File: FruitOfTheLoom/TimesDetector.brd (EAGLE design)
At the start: 113 x 100 mm, 20 parts, among them K1 RELAY-SPDT-JZC-11F, K2 RELAY-SPDT-JZC-11F

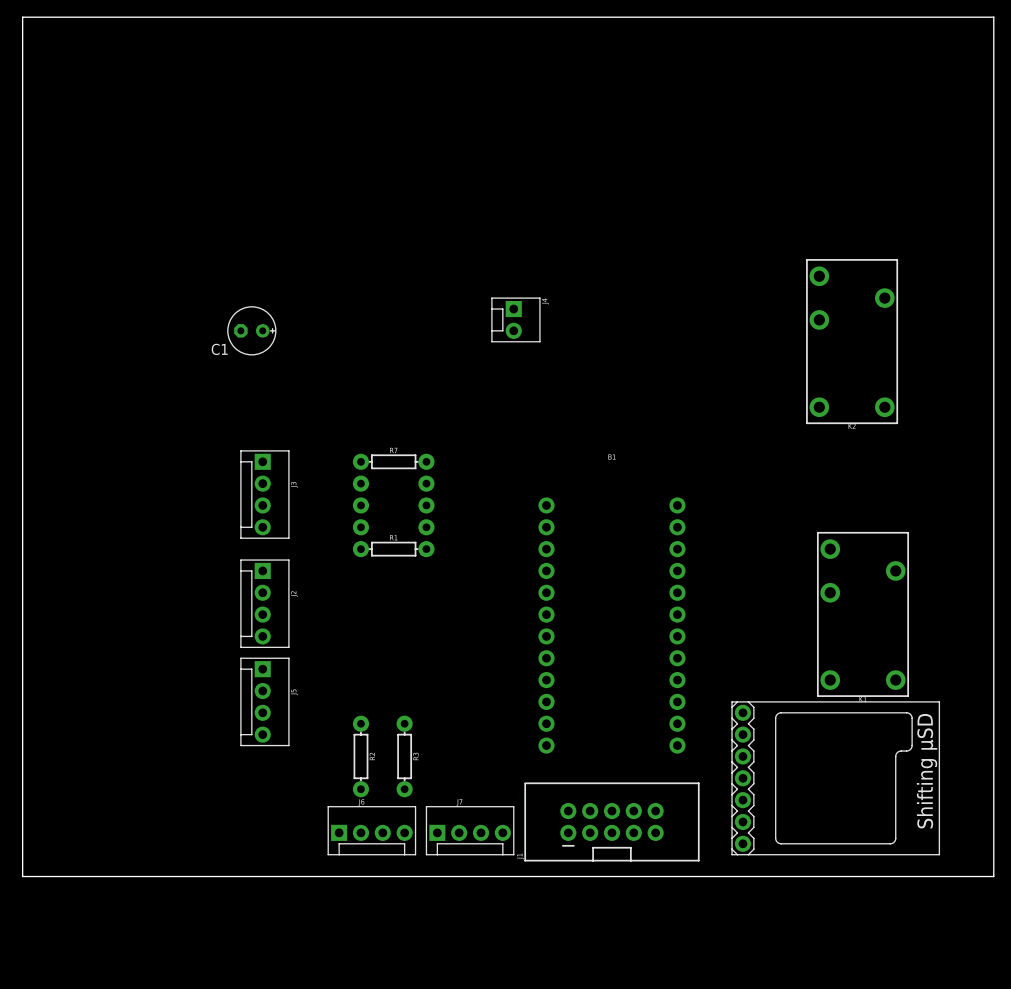
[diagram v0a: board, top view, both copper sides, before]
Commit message: Finalizacion de esquematico, ordenamiento de diseño de placa electronica
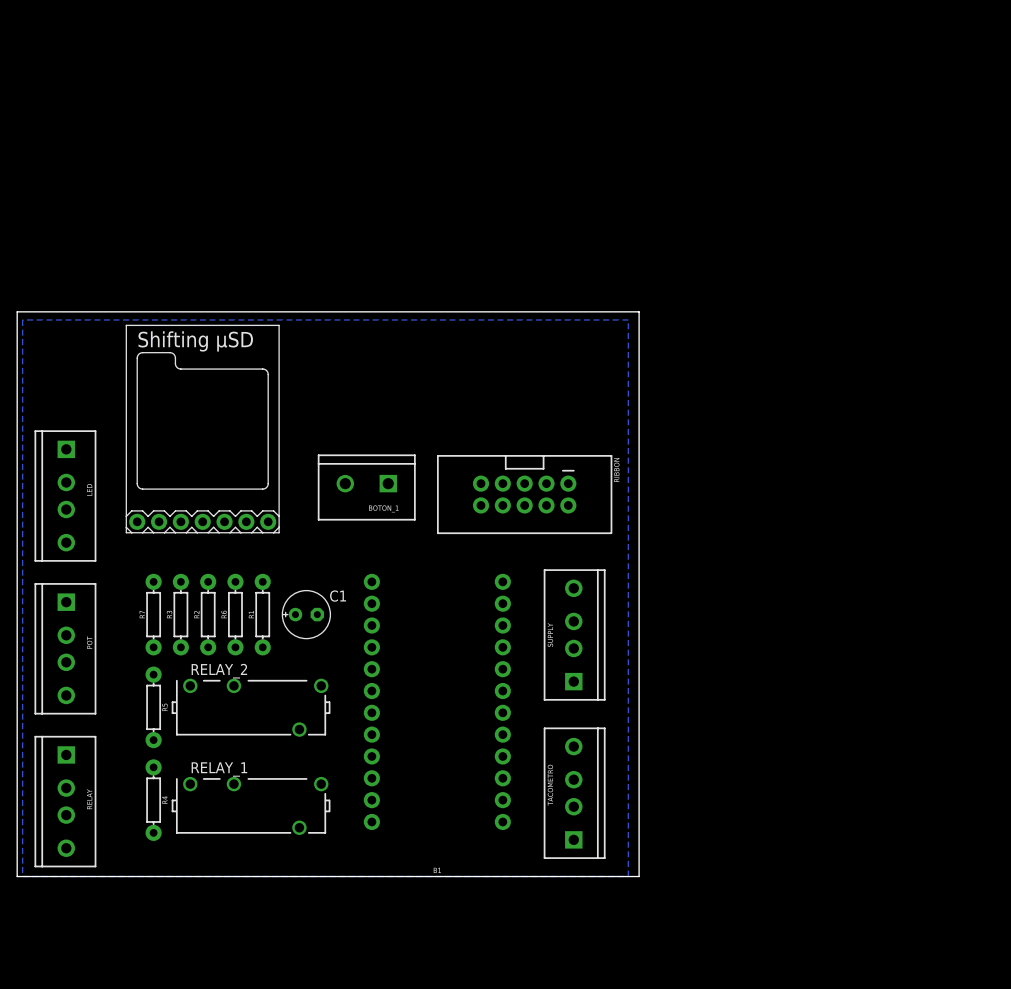
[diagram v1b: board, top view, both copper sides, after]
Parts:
- removed J1: (no value), SparkFun-Connectors:2X5-SHROUDED
- removed J2, J3, J5, J6, J7: (no value), SparkFun-Connectors:MOLEX-1X4
- removed J4: (no value), SparkFun-Connectors:MOLEX-1X2
- removed K1, K2: RELAY-SPDT-JZC-11F, SparkFun-Electromechanical:RELAY-JZC
- added BOTON_1: (no value), SparkFun-Connectors:SCREWTERMINAL-5MM-2
- added LED, POT, RELAY, SUPPLY, TACOMETRO: (no value), SparkFun-Connectors:SCREWTERMINAL-3.5MM-4_LOCK
- added RELAY_1, RELAY_2: G6D-1A-ASI12VDC, relay:G6D
- added RIBBON: (no value), SparkFun-Connectors:2X5-SHROUDED
- C1: value (none) -> 100µ
- moved MODULE1 73.2 mm to (12.1, 40.0), turned to 0 degrees
- moved R4 42.3 mm to (15.2, 8.89), flipped to the top, turned to 270 degrees
- moved R5 36.5 mm to (15.2, 19.7), flipped to the top, turned to 270 degrees
- moved C1 33.6 mm to (33.0, 30.5), turned to 0 degrees
- moved R7 33.1 mm to (15.2, 30.5), turned to 90 degrees
- moved R3 30.8 mm to (18.4, 30.5), turned to 90 degrees
- moved R2 24.3 mm to (21.6, 30.5), turned to 90 degrees
- moved R6 23.9 mm to (24.8, 30.5), flipped to the top, turned to 90 degrees
- moved B1 23.3 mm to (48.3, 19.1), turned to 180 degrees
- moved FRAME1 18.5 mm to (13.3, -8.89)
- moved R1 17.0 mm to (27.9, 30.5), turned to 90 degrees
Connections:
- removed net N$6: MODULE1.P_CD, R6.P$1
- new net N$1: MODULE1.P_CD, R6.P$2
- net A0: now also LED.1; no longer J6.1
- net A1: now also POT.2; no longer J5.2
- net A2: now also RELAY_1.7; no longer K1.4
- net A3: now also R5.P$2, RELAY_2.7; no longer K2.4, R5.P$1
- net D2: now also RIBBON.5; no longer J1.5
- net D3: now also RIBBON.6; no longer J1.6
- net D4: now also RIBBON.7; no longer J1.7
- net D5: now also RIBBON.8; no longer J1.8
- net D6: now also RIBBON.4; no longer J1.4
- net D7: now also RIBBON.3; no longer J1.3
- net D8: now also BOTON_1.2; no longer J4.2
- net D9: now also LED.3; no longer J6.3
- net GND: now also POT.3, R5.P$1, R6.P$1, RELAY.3, RELAY_1.13, RELAY_2.13, RIBBON.9, SUPPLY.2, SUPPLY.4, TACOMETRO.2; no longer J1.9, J2.2, J2.4, J3.2, J5.3, K1.1, K2.1, R5.P$2, R6.P$2
- net IN_SEN_1: now also RELAY.2, RELAY_2.1; no longer J7.2, K1.5
- net IN_SEN_2: now also RELAY.1, RELAY_1.1; no longer J7.1, K2.5
- net N$2: now also LED.4; no longer J6.4
- net N$4: now also LED.2; no longer J6.2
- net N$8: now also R7.P$1, RIBBON.1; no longer J1.1, R7.P$2
- net RX: now also TACOMETRO.3; no longer J3.3
- net TX: now also TACOMETRO.4; no longer J3.4
- net V0: now also POT.4, RIBBON.2; no longer J1.2, J5.4
- net VCC: now also RELAY.4, RELAY_1.5, RELAY_2.5, SUPPLY.1, TACOMETRO.1; no longer J2.1, J3.1, J7.4
- net VCC_O: now also BOTON_1.1, POT.1, R7.P$2, RIBBON.10, SUPPLY.3; no longer J1.10, J2.3, J4.1, J5.1, K1.3, K2.3, R7.P$1
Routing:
- added copper zone on layer 16, net GND
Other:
- board size 113 x 100 mm -> 72.4 x 65.7 mm

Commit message: Orden de los componentes segun el cliente
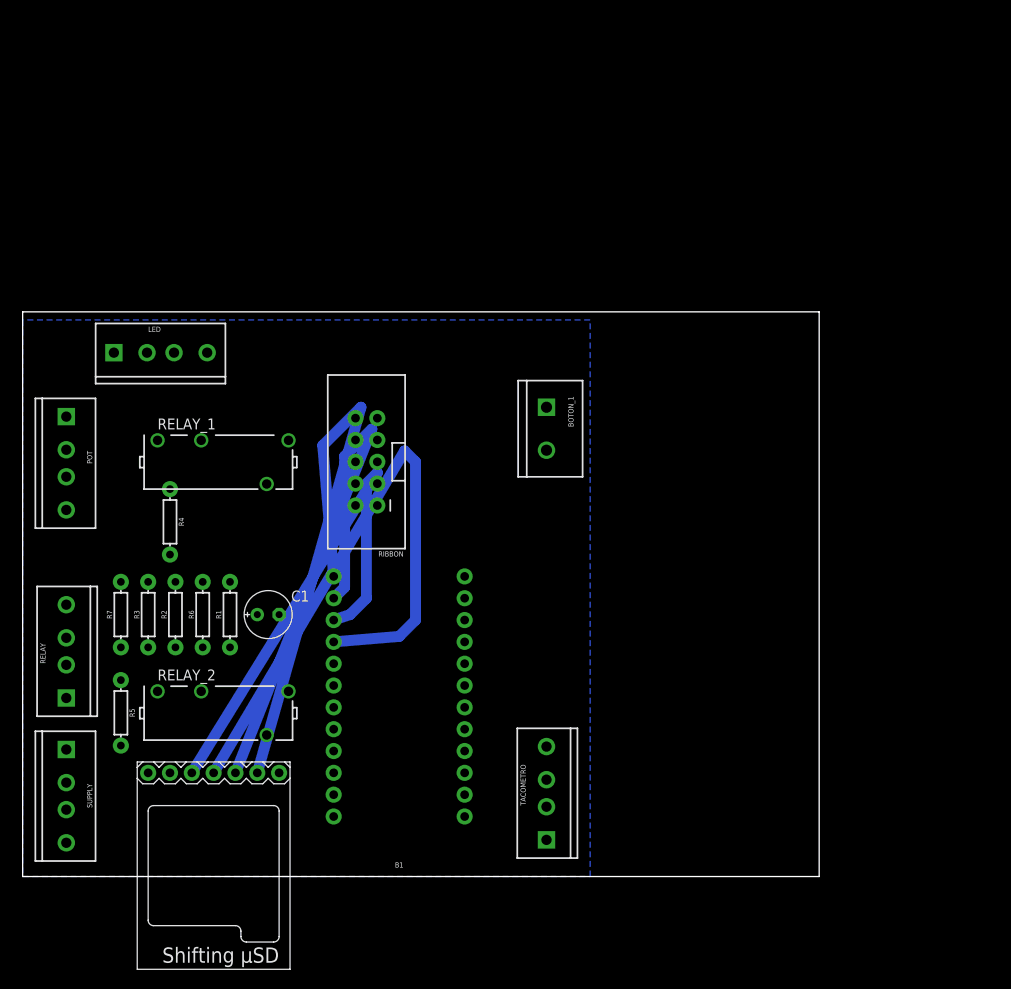
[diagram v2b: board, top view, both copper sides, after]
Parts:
- moved SUPPLY 59.6 mm to (5.08, 14.6), turned to 270 degrees
- moved RELAY_1 40.2 mm to (22.9, 48.3)
- moved MODULE1 32.8 mm to (31.1, 13.3), turned to 180 degrees
- moved R4 32.4 mm to (17.1, 41.3)
- moved POT 21.6 mm to (5.08, 53.3)
- moved BOTON_1 20.4 mm to (61.0, 54.6), turned to 270 degrees
- moved RIBBON 18.8 mm to (40.0, 48.3), turned to 180 degrees
- moved LED 12.8 mm to (10.8, 61.0), turned to 0 degrees
- moved RELAY 6.98 mm to (5.08, 21.0), turned to 90 degrees
- moved B1 4.49 mm to (43.8, 19.7)
- moved C1 4.45 mm to (28.6, 30.5)
- moved RELAY_2 3.86 mm to (22.9, 19.1)
- moved R5 3.86 mm to (11.4, 19.1)
- moved R1 3.81 mm to (24.1, 30.5)
- moved R6 3.81 mm to (21.0, 30.5)
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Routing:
- net D13: track 0.00 -> 74.1 mm
- net D10: track 0.00 -> 65.8 mm
- net D11: track 0.00 -> 64.6 mm
- net D12: track 0.00 -> 60.9 mm
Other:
- board size 72.4 x 65.7 mm -> 92.7 x 65.7 mm

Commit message: Finalizacion de diseño de circuito, fase de revision
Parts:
- added FRAME3: FRAME-LETTERNO_PACKAGE, SparkFun-Aesthetics:DUMMY
- added J2: (no value), SparkFun-Connectors:1X05_LONGPADS
- moved RELAY_2 51.0 mm to (66.7, 45.1), turned to 90 degrees
- moved R5 45.8 mm to (51.4, 41.3)
- moved R1 42.0 mm to (66.0, 33.7), turned to 180 degrees
- moved C1 36.3 mm to (64.8, 27.3), turned to 270 degrees
- moved RELAY_1 35.1 mm to (57.8, 45.1), turned to 90 degrees
- moved R4 29.8 mm to (47.0, 41.3), turned to 90 degrees
- moved R7 29.4 mm to (8.26, 59.7), turned to 180 degrees
- moved R2 27.7 mm to (8.26, 56.5), turned to 0 degrees
- moved R3 23.7 mm to (8.26, 53.3), turned to 0 degrees
- moved POT 15.9 mm to (6.35, 37.5), turned to 90 degrees
- moved MODULE1 13.1 mm to (36.2, 25.4)
- moved TACOMETRO 12.0 mm to (67.3, 14.6), turned to 270 degrees
- moved SUPPLY 10.9 mm to (6.35, 3.81), turned to 90 degrees
- moved BOTON_1 10.2 mm to (66.0, 63.5)
- moved RELAY 10.2 mm to (6.35, 31.1), turned to 270 degrees
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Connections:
- net D2: now also J2.5
- net D3: now also J2.4
- net D5: now also J2.3
- net D6: now also J2.2
- net D9: now also J2.1
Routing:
- net VCC_O: track 0.00 -> 181.3 mm
- net D2: track 0.00 -> 150.1 mm
- net VCC: track 0.00 -> 144.1 mm
- net IN_SEN_1: track 0.00 -> 113.9 mm
- net IN_SEN_2: track 0.00 -> 94.2 mm
- net D4: track 0.00 -> 77.0 mm
- net D9: track 0.00 -> 66.3 mm
- net V0: track 0.00 -> 65.1 mm
- net A0: track 0.00 -> 61.1 mm
- net D13: track 74.1 -> 16.0 mm
- net D3: track 0.00 -> 57.0 mm
- net A1: track 0.00 -> 53.2 mm
- net D10: track 65.8 -> 15.8 mm
- net D7: track 0.00 -> 49.7 mm
- net A3: track 0.00 -> 46.4 mm
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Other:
- board size 92.7 x 65.7 mm -> 73 x 68.9 mm

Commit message: Finalizacion de diseño de circuito, fase de revision
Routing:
- net VCC_O: track 181.3 -> 182.8 mm
- net A0: track 61.1 -> 61.8 mm
- net A1: track 53.2 -> 54.0 mm
- added copper zone on layer 1, net GND
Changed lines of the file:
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@@
 <contactref element="R5" pad="P$1"/>
 <contactref element="RELAY" pad="3"/>
-<polygon width="0.1524" layer="16">
+<polygon width="0.1524" layer="16" isolate="0.6096">
 <vertex x="-0.635" y="68.58"/>
 <vertex x="-0.635" y="0"/>
@@
 <contactref element="R6" pad="P$1"/>
 <contactref element="R4" pad="P$2"/>
+<polygon width="0.0762" layer="1" isolate="0.6096">
+<vertex x="-0.635" y="68.58"/>
+<vertex x="-0.635" y="0"/>
+<vertex x="72.39" y="0"/>
+<vertex x="72.39" y="68.58"/>
+</polygon>
 </signal>
 <signal name="RX">
@@
 <wire x1="9.6572" y1="41.1428" x2="11.43" y2="39.37" width="0.8128" layer="16"/>
 <wire x1="40.005" y1="20.32" x2="38.735" y2="20.32" width="0.8128" layer="16"/>
-<wire x1="38.735" y1="20.32" x2="38.1" y2="19.685" width="0.8128" layer="16"/>
-<wire x1="13.335" y1="19.685" x2="38.1" y2="19.685" width="0.8128" layer="16"/>
-<wire x1="11.43" y1="21.59" x2="13.335" y2="19.685" width="0.8128" layer="16"/>
+<wire x1="38.735" y1="20.32" x2="37.465" y2="19.05" width="0.8128" layer="16"/>
+<wire x1="13.335" y1="19.05" x2="37.465" y2="19.05" width="0.8128" layer="16"/>
+<wire x1="11.43" y1="21.59" x2="13.335" y2="19.05" width="0.8128" layer="16"/>
 </signal>
 <signal name="V0">
@@
 <contactref element="B1" pad="17"/>
 <wire x1="40.005" y1="22.86" x2="38.735" y2="22.86" width="0.8128" layer="16"/>
-<wire x1="38.735" y1="22.86" x2="37.465" y2="21.59" width="0.8128" layer="16"/>
-<wire x1="37.465" y1="21.59" x2="15.875" y2="21.59" width="0.8128" layer="16"/>
+<wire x1="38.735" y1="22.86" x2="36.83" y2="20.955" width="0.8128" layer="16"/>
+<wire x1="36.83" y1="20.955" x2="15.875" y2="20.955" width="0.8128" layer="16"/>
 <wire x1="17.6022" y1="55.245" x2="15.875" y2="55.245" width="0.8128" layer="16"/>
 <wire x1="15.875" y1="55.245" x2="14.605" y2="53.975" width="0.8128" layer="16"/>
-<wire x1="14.605" y1="22.86" x2="15.875" y2="21.59" width="0.8128" layer="16"/>
+<wire x1="14.605" y1="22.86" x2="15.875" y2="20.955" width="0.8128" layer="16"/>
 <wire x1="14.605" y1="53.975" x2="14.605" y2="22.86" width="0.8128" layer="16"/>
 </signal>
@@
 <contactref element="MODULE1" pad="P_VCC"/>
 <contactref element="R7" pad="P$2"/>
-<wire x1="4.445" y1="59.69" x2="5.715" y2="59.69" width="0.8128" layer="1"/>
+<wire x1="4.445" y1="59.69" x2="6.35" y2="59.69" width="0.8128" layer="1"/>
 <wire x1="6.35" y1="37.2872" x2="8.4328" y2="37.2872" width="0.8128" layer="16"/>
 <wire x1="9.525" y1="36.195" x2="8.4328" y2="37.2872" width="0.8128" layer="16"/>
-<wire x1="6.35" y1="37.2872" x2="6.1722" y2="37.465" width="0.8128" layer="1"/>
-<wire x1="6.1722" y1="37.465" x2="5.08" y2="37.465" width="0.8128" layer="1"/>
-<wire x1="5.08" y1="37.465" x2="3.81" y2="38.735" width="0.8128" layer="1"/>
-<wire x1="3.81" y1="38.735" x2="3.81" y2="49.53" width="0.8128" layer="1"/>
-<wire x1="3.81" y1="49.53" x2="5.08" y2="50.8" width="0.8128" layer="1"/>
+<wire x1="5.08" y1="50.8" x2="3.81" y2="49.53" width="0.8128" layer="1"/>
 <wire x1="6.35" y1="50.8" x2="7.62" y2="52.07" width="0.8128" layer="1"/>
 <wire x1="7.62" y1="58.42" x2="6.35" y2="59.69" width="0.8128" layer="1"/>
@@
 <wire x1="34.925" y1="13.97" x2="36.195" y2="12.7" width="0.8128" layer="1"/>
 <wire x1="36.195" y1="12.7" x2="40.005" y2="12.7" width="0.8128" layer="1"/>
-<wire x1="35.56" y1="63.5" x2="66.04" y2="63.5" width="0.8128" layer="1"/>
+<wire x1="35.56" y1="64.135" x2="63.5" y2="64.135" width="0.8128" layer="1"/>
+<wire x1="63.5" y1="64.135" x2="64.135" y2="63.5" width="0.8128" layer="1"/>
+<wire x1="64.135" y1="63.5" x2="66.04" y2="63.5" width="0.8128" layer="1"/>
 <wire x1="37.465" y1="53.975" x2="34.925" y2="53.975" width="0.8128" layer="1"/>
 <wire x1="34.925" y1="53.975" x2="34.29" y2="54.61" width="0.8128" layer="1"/>
-<wire x1="34.29" y1="54.61" x2="34.29" y2="62.23" width="0.8128" layer="1"/>
-<wire x1="34.29" y1="62.23" x2="35.56" y2="63.5" width="0.8128" layer="1"/>
-<wire x1="33.02" y1="63.5" x2="34.29" y2="62.23" width="0.8128" layer="1"/>
-<wire x1="5.715" y1="59.69" x2="6.35" y2="59.69" width="0.8128" layer="1"/>
+<wire x1="34.29" y1="54.61" x2="34.29" y2="62.865" width="0.8128" layer="1"/>
+<wire x1="34.29" y1="62.865" x2="35.56" y2="64.135" width="0.8128" layer="1"/>
+<wire x1="33.02" y1="64.135" x2="34.29" y2="62.865" width="0.8128" layer="1"/>
 <wire x1="6.35" y1="59.69" x2="7.62" y2="60.96" width="0.8128" layer="1"/>
 <wire x1="7.62" y1="60.96" x2="7.62" y2="62.865" width="0.8128" layer="1"/>
-<wire x1="7.62" y1="62.865" x2="8.255" y2="63.5" width="0.8128" layer="1"/>
-<wire x1="8.255" y1="63.5" x2="33.02" y2="63.5" width="0.8128" layer="1"/>
+<wire x1="7.62" y1="62.865" x2="8.89" y2="64.135" width="0.8128" layer="1"/>
+<wire x1="8.89" y1="64.135" x2="33.02" y2="64.135" width="0.8128" layer="1"/>
+<wire x1="3.81" y1="49.53" x2="3.81" y2="38.1" width="0.8128" layer="1"/>
+<wire x1="4.6228" y1="37.2872" x2="6.35" y2="37.2872" width="0.8128" layer="1"/>
+<wire x1="3.81" y1="38.1" x2="4.6228" y2="37.2872" width="0.8128" layer="1"/>
 </signal>
 <signal name="N$8">
